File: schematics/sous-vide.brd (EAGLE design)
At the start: 81.3 x 81.3 mm, 33 parts, among them IC1 MEGA32-P

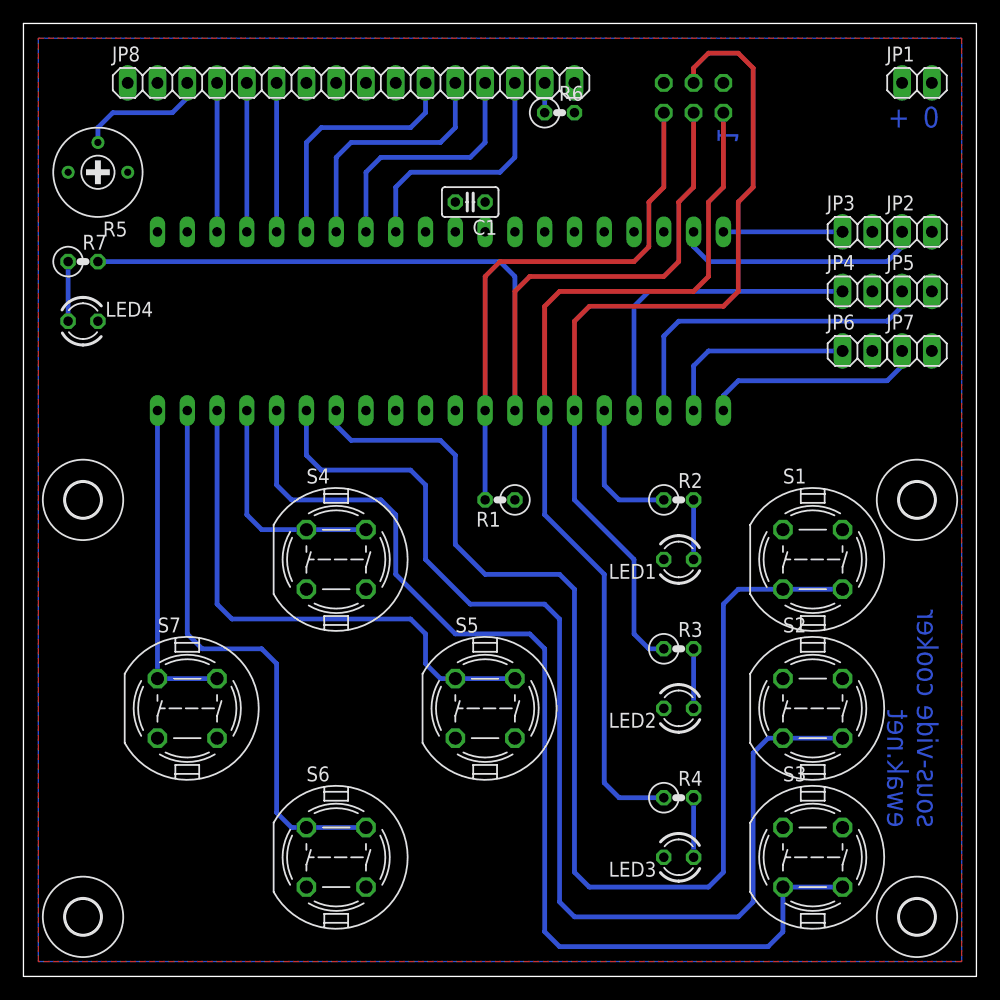
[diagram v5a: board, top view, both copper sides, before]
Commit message: Switched to ATmega328 and updated schematics and board.
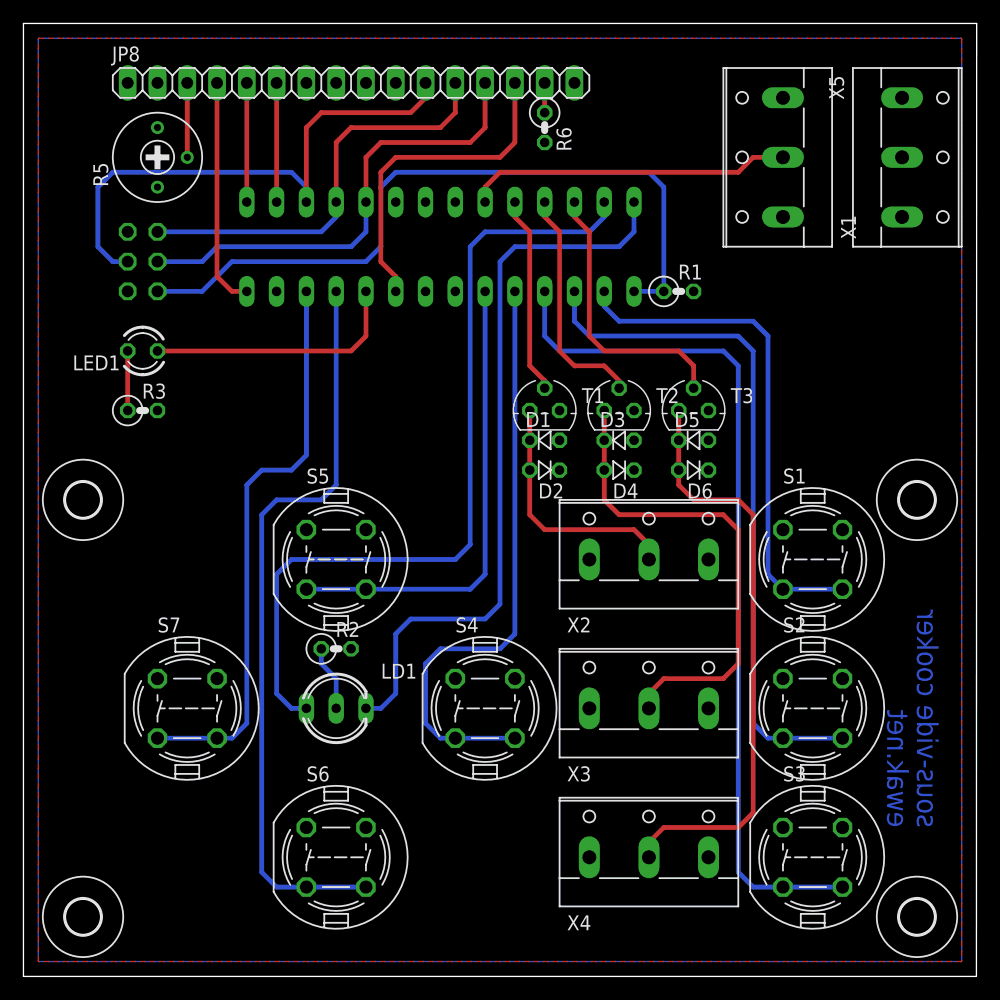
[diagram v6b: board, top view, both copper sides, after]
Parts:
- removed C1: (no value), resistor:C025-025X050
- removed IC1: MEGA32-P, atmel:DIL40
- removed JP1: Power, pinhead:1X02
- removed JP2, JP3: Sensor, pinhead:1X02
- removed JP4, JP5: aux, pinhead:1X02
- removed JP6: heater, pinhead:1X02
- removed JP7: pump, pinhead:1X02
- removed LED2, LED3, LED4: (no value), led:LED3MM
- removed R4, R7: 330, rcl:0207/2V
- added D1, D2, D3, D4, D5, D6: (no value), diode:D-2.5
- added IC2: MEGA8-P, atmel:DIL28-3
- added LD1: (no value), led:DUOLED-C-5MM
- added T1, T2, T3: BC547, transistor:TO92
- added X1, X2, X3, X4, X5: (no value), con-wago-508:W237-133
- moved R3 50.0 mm to (10.2, 48.3)
- moved LED1 49.1 mm to (10.2, 53.3)
- moved JP9 49.0 mm to (10.2, 61.0), turned to 270 degrees
- moved R2 31.9 mm to (26.7, 27.9)
- moved R1 23.4 mm to (55.9, 58.4), turned to 0 degrees
- moved S4 18.0 mm to (39.4, 22.9)
- moved S5 18.0 mm to (26.7, 35.6)
- moved R5 5.24 mm to (11.4, 69.8), turned to 90 degrees
- moved R6 1.80 mm to (44.5, 72.4), turned to 270 degrees
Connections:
- removed net BUTTON0: IC1.14, S1.3, S1.4
- removed net BUTTON1: IC1.15, S2.3, S2.4
- removed net BUTTON2: IC1.16, S3.3, S3.4
- removed net BUTTON3: IC1.17, S4.1, S4.2
- removed net BUTTON4: IC1.18, S5.1, S5.2
- removed net BUTTON5: IC1.19, S6.1, S6.2
- removed net BUTTON6: IC1.20, S7.1, S7.2
- removed net BUTTON7: IC1.21
- removed net DISPLAY0: IC1.22
- removed net DISPLAY1: IC1.23, JP8.4
- removed net DISPLAY2: IC1.24, JP8.5
- removed net DISPLAY3: IC1.25, JP8.6
- removed net DISPLAY4: IC1.26, JP8.11
- removed net DISPLAY5: IC1.27, JP8.12
- removed net DISPLAY6: IC1.28, JP8.13
- removed net DISPLAY7: IC1.29, JP8.14
- removed net N$10: IC1.5, R2.1
- removed net N$11: IC1.6, JP9.4, R3.1
- removed net N$12: IC1.40, JP3.1
- removed net N$13: IC1.7, JP9.1, R4.1
- removed net N$16: LED4.A, R7.1
- removed net N$17: IC1.8, JP9.3, R7.2
- new net N$18: IC2.19, JP8.13, JP9.3
- new net N$19: IC2.18, JP8.12, JP9.1
- new net N$20: IC2.14, JP8.4
- new net N$21: IC2.15, JP8.5
- new net N$22: IC2.16, JP8.6
- new net N$23: IC2.9, JP8.14
- new net N$24: IC2.17, JP8.11, JP9.4
- new net N$26: IC2.12, S7.3, S7.4
- new net N$28: IC2.11, S6.3, S6.4
- new net N$29: D5.C, D6.A, T3.3, X4.2
- new net N$30: IC2.5, S4.3, S4.4
- new net N$31: IC2.1, JP9.5, R1.1
- new net N$32: IC2.6, S5.3, S5.4
- new net N$33: D3.C, D4.A, T2.3, X3.2
- new net N$34: D1.C, D2.A, T1.3, X2.2
- new net N$35: IC2.4, S3.3, S3.4
- new net N$36: IC2.2, S1.3, S1.4
- new net N$37: IC2.3, S2.3, S2.4
- net GND: now also D1.A, D3.A, D5.A, IC2.22, IC2.8, R2.2, R3.2, S4.1, S4.2, S5.1, S5.2, S6.1, S6.2, S7.1, S7.2, T1.1, T2.1, T3.1, X1.3, X2.3, X3.3, X4.3, X5.3; no longer C1.2, IC1.11, IC1.31, JP1.2, JP2.2, JP3.2, JP4.2, JP5.2, JP6.2, JP7.2, LED1.K, LED2.K, LED3.K, LED4.K, S4.3, S4.4, S5.3, S5.4, S6.3, S6.4, S7.3, S7.4
- net N$1: now also LED1.K, R3.1; no longer IC1.1, JP7.1
- net N$2: now also IC2.10, LED1.A; no longer IC1.2, JP6.1
- net N$3: now also IC2.23, X1.2; no longer IC1.9, JP9.5, R1.2
- net N$4: now also IC2.24, T1.2; no longer IC1.3, JP5.1
- net N$5: now also IC2.25, T2.2; no longer IC1.4, JP4.1
- net N$6: now also IC2.26, T3.2; no longer IC1.39, JP2.1
- net N$7: now also LD1.C, R2.1; no longer LED3.A, R4.2
- net N$8: now also IC2.28, LD1.AR; no longer LED2.A, R3.2
- net N$9: now also IC2.27, LD1.AX; no longer LED1.A, R2.2
- net VCC: now also D2.C, D4.C, D6.C, IC2.20, IC2.21, IC2.7, R1.2, X1.1, X2.1, X3.1, X4.1, X5.1; no longer C1.1, IC1.10, IC1.30, IC1.32, JP1.1, R1.1
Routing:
- net BUTTON0: track 103.3 -> 0.00 mm
- net BUTTON1: track 97.4 -> 0.00 mm
- net BUTTON2: track 92.4 -> 0.00 mm
- net N$17: track 85.9 -> 0.00 mm
- net N$13: track 77.9 -> 0.00 mm
- net N$35: track 0.00 -> 74.0 mm
- net N$11: track 73.8 -> 0.00 mm
- net N$9: track 5.08 -> 69.9 mm
- net N$28: track 0.00 -> 63.8 mm
- net N$31: track 0.00 -> 62.3 mm
- net N$37: track 0.00 -> 58.7 mm
- net N$8: track 5.08 -> 62.3 mm
- net N$30: track 0.00 -> 51.1 mm
- net N$29: track 0.00 -> 50.4 mm
- net N$26: track 0.00 -> 48.6 mm
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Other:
- board text removed: "+"
- board text removed: "0"
- board text removed: "1"

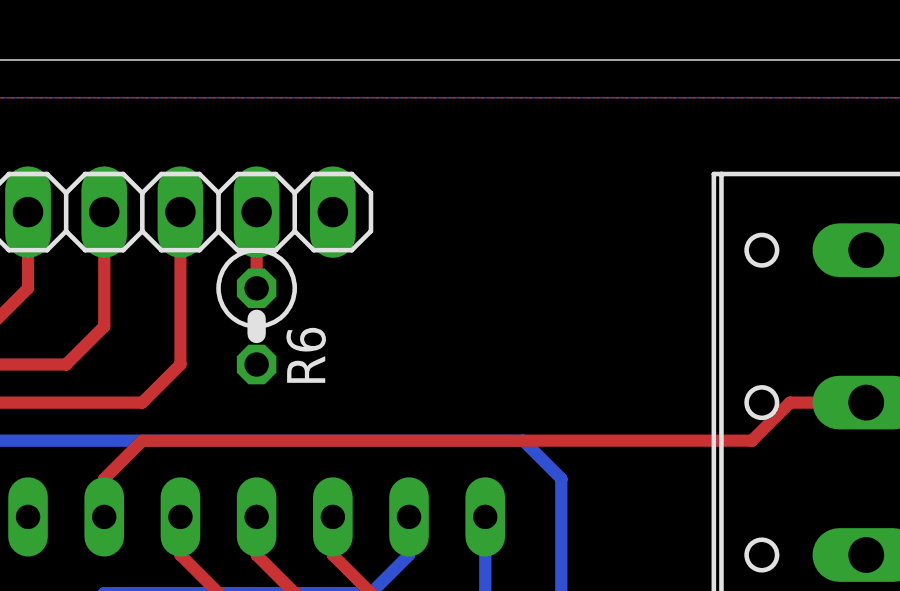
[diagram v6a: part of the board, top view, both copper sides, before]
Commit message: Moved R6 on board for symmetry with R1.
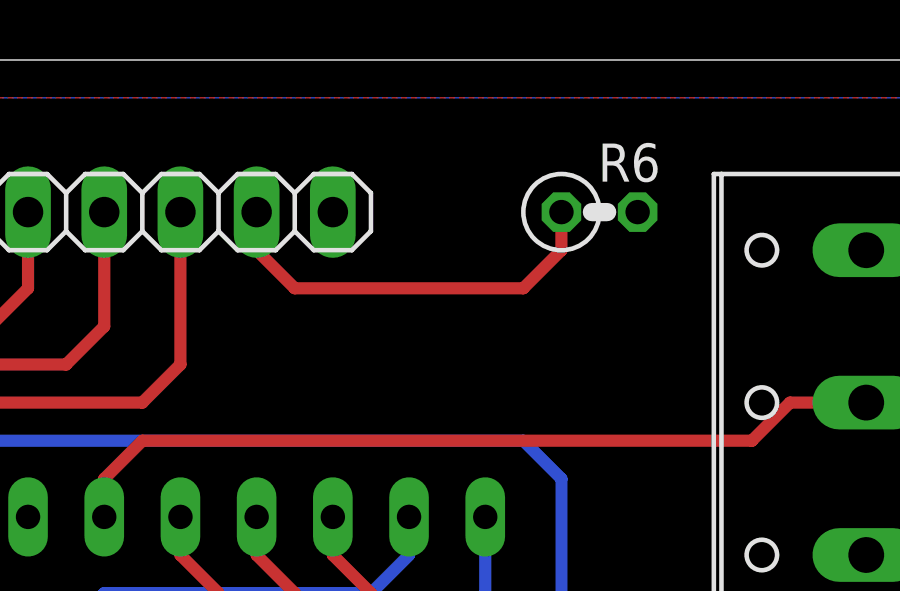
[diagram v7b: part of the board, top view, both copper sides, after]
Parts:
- moved R6 12.0 mm to (55.9, 76.2), turned to 0 degrees
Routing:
- net N$15: track 2.54 -> 13.8 mm
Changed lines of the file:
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@@
 <element name="R2" library="rcl" package="0207/2V" value="330" x="26.67" y="27.94"/>
 <element name="R5" library="resistor" package="RTRIM3339P" value="" x="11.43" y="69.85" rot="R90"/>
-<element name="R6" library="rcl" package="0207/2V" value="330" x="44.45" y="72.39" rot="R270"/>
+<element name="R6" library="rcl" package="0207/2V" value="330" x="55.88" y="76.2"/>
 <element name="H1" library="holes" package="3,0" value="MOUNT-HOLE3.0" x="76.2" y="5.08"/>
 <element name="H2" library="holes" package="3,0" value="MOUNT-HOLE3.0" x="5.08" y="40.64"/>
@@
 <contactref element="R6" pad="1"/>
 <contactref element="JP8" pad="15"/>
-<wire x1="44.45" y1="73.66" x2="44.45" y2="76.2" width="0.4064" layer="1"/>
+<wire x1="54.61" y1="76.2" x2="54.61" y2="74.93" width="0.4064" layer="1"/>
+<wire x1="54.61" y1="74.93" x2="53.34" y2="73.66" width="0.4064" layer="1"/>
+<wire x1="53.34" y1="73.66" x2="45.72" y2="73.66" width="0.4064" layer="1"/>
+<wire x1="45.72" y1="73.66" x2="44.45" y2="74.93" width="0.4064" layer="1"/>
+<wire x1="44.45" y1="74.93" x2="44.45" y2="76.2" width="0.4064" layer="1"/>
 </signal>
 <signal name="N$26">

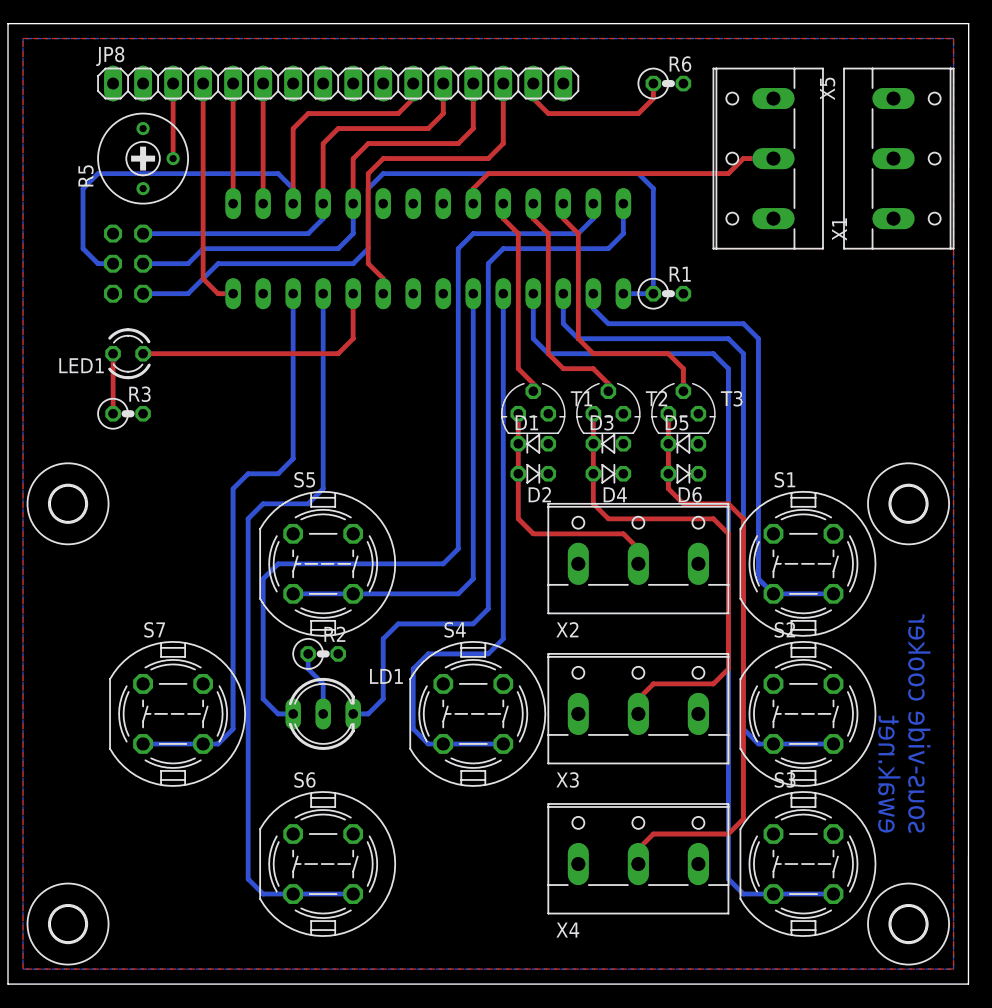
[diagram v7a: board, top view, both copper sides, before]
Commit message: Changed connectors and renumbered parts on schematic and board.
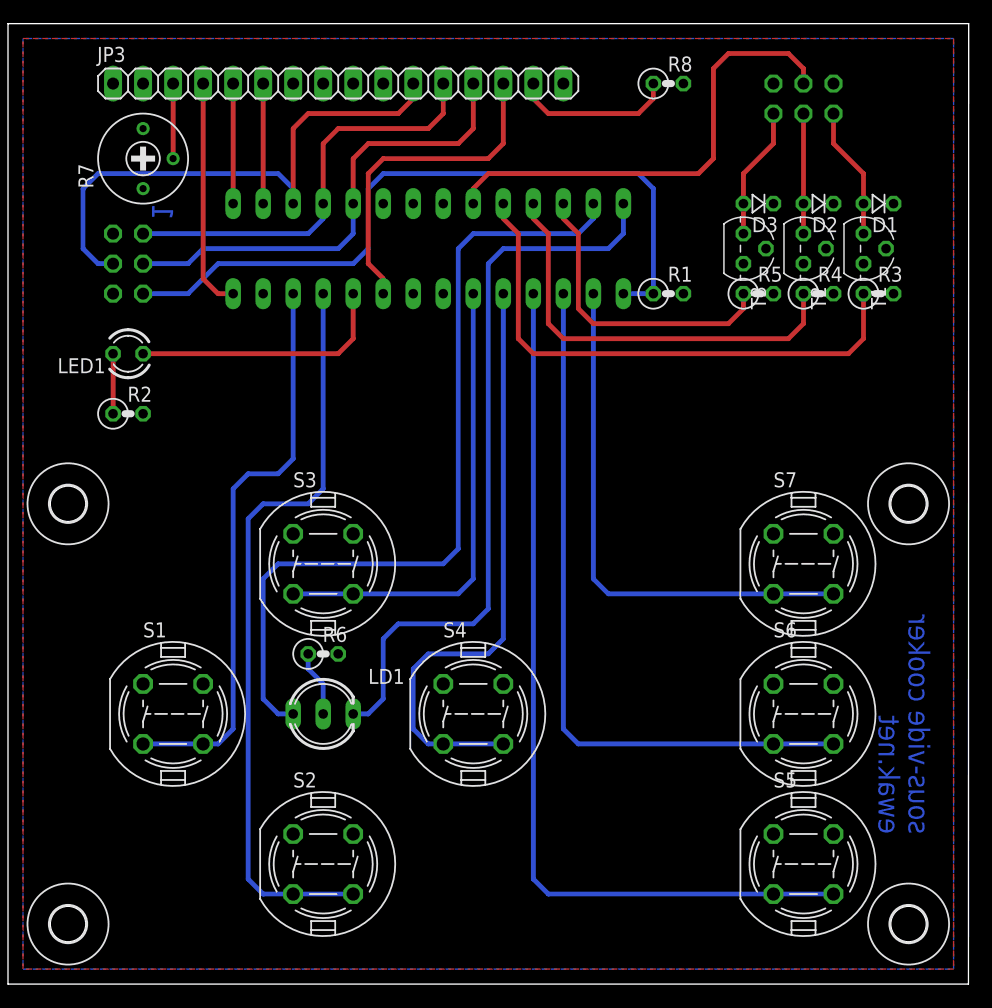
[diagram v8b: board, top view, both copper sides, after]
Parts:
- removed D4, D5, D6: (no value), diode:D-2.5
- removed X1, X2, X3, X4, X5: (no value), con-wago-508:W237-133
- added JP2: ISP, pinhead:2X03
- added R4, R8: 330, rcl:0207/2V
- added R7: (no value), resistor:RTRIM3339P
- R5: value (none) -> 330; device resistor:RTRIM3339P -> rcl:0207/2V
- moved R3 64.3 mm to (73.7, 58.4)
- moved R6 56.4 mm to (26.7, 27.9)
- moved S1 54.8 mm to (14.0, 22.9)
- moved S7 54.8 mm to (67.3, 35.6)
- moved R5 53.3 mm to (63.5, 58.4), turned to 0 degrees
- moved S3 47.9 mm to (26.7, 35.6)
- moved S5 47.9 mm to (67.3, 10.2)
- moved S2 42.6 mm to (26.7, 10.2)
- moved S6 42.6 mm to (67.3, 22.9)
- moved D1 35.6 mm to (73.7, 66.0), turned to 180 degrees
- moved D2 33.2 mm to (68.6, 66.0)
- moved T1 31.2 mm to (72.4, 62.2), turned to 270 degrees
- moved R2 26.2 mm to (10.2, 48.3)
- moved D3 24.0 mm to (63.5, 66.0), turned to 180 degrees
- moved T2 21.6 mm to (67.3, 62.2), turned to 270 degrees
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- renumbered IC2 to IC1, JP8 to JP3, JP9 to JP1
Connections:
- removed net N$29: D5.C, D6.A, T3.3, X4.2
- removed net N$33: D3.C, D4.A, T2.3, X3.2
- removed net N$34: D1.C, D2.A, T1.3, X2.2
- new net N$10: R3.2, T1.2
- new net N$11: R4.2, T2.2
- new net N$12: R5.2, T3.2
- new net N$13: D1.A, JP2.6, T1.3
- new net N$16: D2.A, JP2.4, T2.3
- new net N$17: D3.A, JP2.2, T3.3
- net GND: now also JP2.5, R6.2, R7.3; no longer D1.A, D3.A, D5.A, R3.2, R5.3, X1.3, X2.3, X3.3, X4.3, X5.3
- net N$1: now also R2.1; no longer R3.1
- net N$14: now also R7.2; no longer R5.2
- net N$15: now also R8.1; no longer R6.1
- net N$26: now also S1.3, S1.4; no longer S7.3, S7.4
- net N$28: now also S2.3, S2.4; no longer S6.3, S6.4
- net N$3: now also JP2.3; no longer X1.2
- net N$32: now also S3.3, S3.4; no longer S5.3, S5.4
- net N$35: now also S5.3, S5.4; no longer S3.3, S3.4
- net N$36: now also S7.3, S7.4; no longer S1.3, S1.4
- net N$37: now also S6.3, S6.4; no longer S2.3, S2.4
- net N$4: now also R3.1; no longer T1.2
- net N$5: now also R4.1; no longer T2.2
- net N$6: now also R5.1; no longer T3.2
- net N$7: now also R6.1; no longer R2.1
- net VCC: now also D1.C, D3.C, JP2.1, R7.1, R8.2; no longer D4.C, D6.C, R5.1, R6.2, X1.1, X2.1, X3.1, X4.1, X5.1
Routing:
- net N$29: track 50.4 -> 0.00 mm
- net N$33: track 41.5 -> 0.00 mm
- net N$4: track 16.9 -> 46.0 mm
- net N$34: track 21.4 -> 0.00 mm
- net N$5: track 20.0 -> 35.9 mm
- net N$3: track 27.7 -> 40.2 mm
- net N$13: track 0.00 -> 11.2 mm
- net N$17: track 0.00 -> 11.2 mm
- net N$16: track 0.00 -> 10.2 mm
- net N$6: track 23.8 -> 25.7 mm
- net N$36: track 43.5 -> 45.0 mm
- net N$37: track 58.7 -> 60.2 mm
- net N$35: track 74.0 -> 75.5 mm
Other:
- board text added: "1"
